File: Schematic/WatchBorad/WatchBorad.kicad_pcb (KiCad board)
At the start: 4 copper layers, 35 x 35 mm, 113 parts, among them J1 Conn_01x07_Female, J3 TYPE-C-31-M-17, M1 Motor_DC, SW1 SW_Push, SW2 SW_Push, SW3 SW_Push, SW4 SW_Push, SW5 SW_Push, U1 PQFN50P300X250X86-14N, U10 TPS62740DSST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

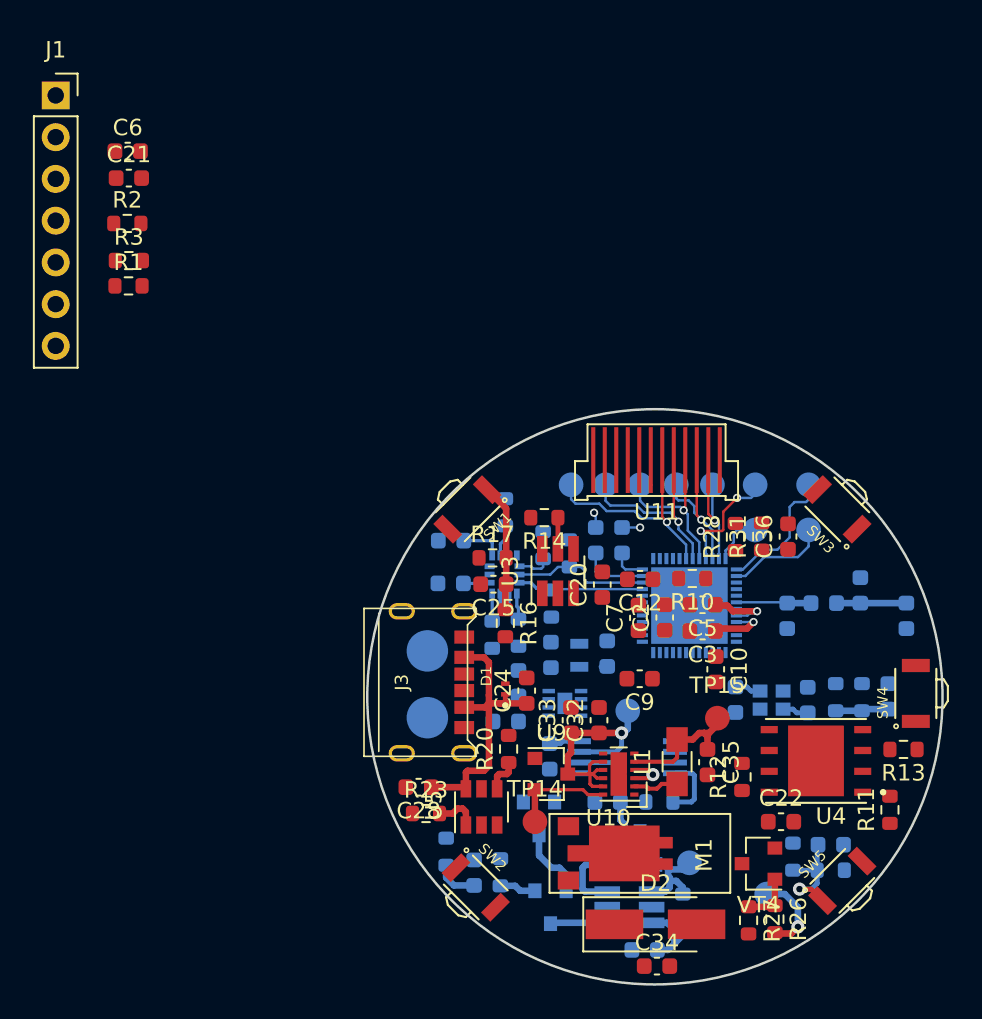
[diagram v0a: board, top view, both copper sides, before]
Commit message: Fixed board's proposals. Fixed testpoints' footprint. Fixed DRC violations. Added +5V testpoint
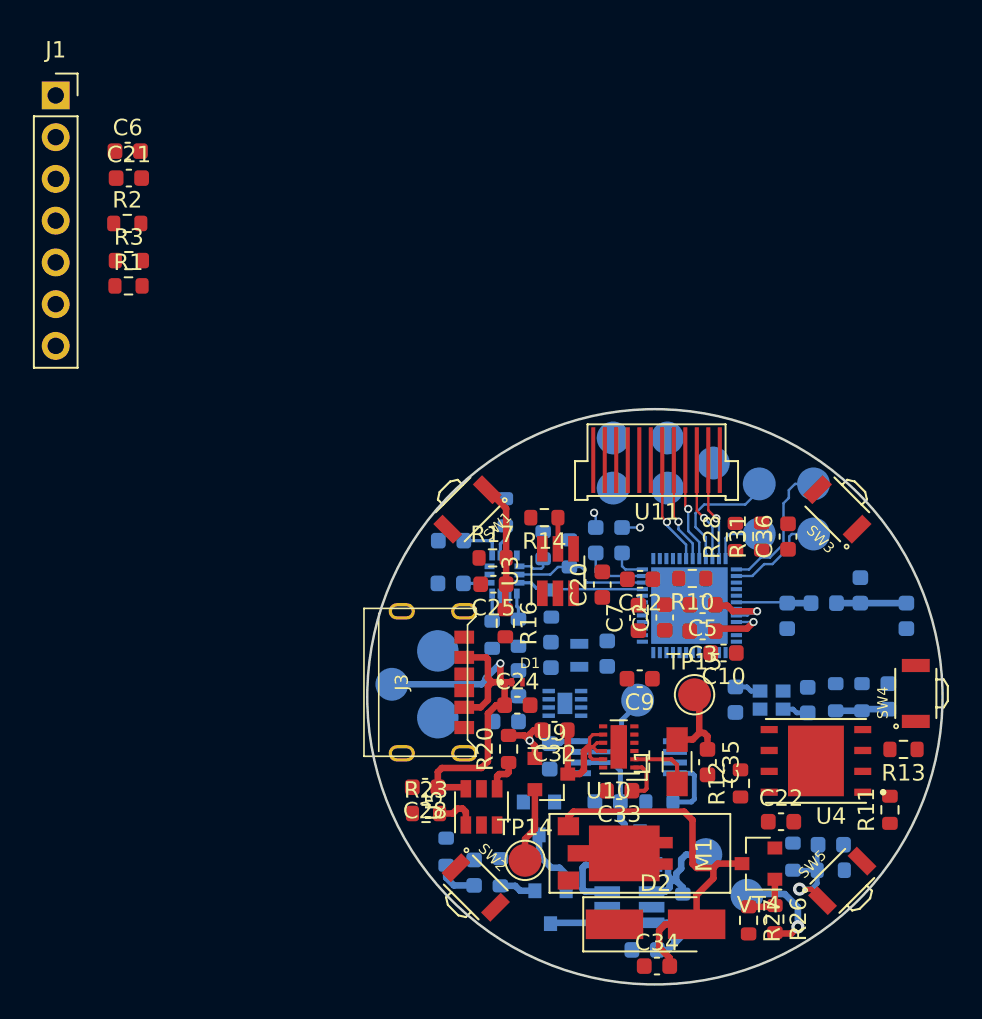
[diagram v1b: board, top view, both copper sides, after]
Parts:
- added TP5: TestPoint, TestPoint:TestPoint_Pad_D2.0mm, B.Cu at (72.9, 88.1)
- TP1, TP10, TP11, TP12, TP13, TP14, TP15, TP2, TP3, TP4, TP6, TP7, TP8, TP9: footprint Measurement_Points:Measurement_Point_Round-SMD-Pad_Small -> TestPoint:TestPoint_Pad_D2.0mm
- U1: value PQFN50P300X250X86-14N -> LSM6DSLTR
- moved C33 5.19 mm to (86.7, 94.6), turned to 180 degrees
- moved TP8 3.83 mm to (86.4, 73.2)
- moved TP7 3.30 mm to (89.7, 73.2)
- moved C32 2.78 mm to (82.8, 90.9), turned to 180 degrees
- moved TP14 2.43 mm to (81.0, 98.8)
- moved TP15 1.99 mm to (91.3, 88.8)
- moved U10 1.65 mm to (86.7, 91.9)
- moved TP10 1.33 mm to (92.5, 74.7)
- moved TP13 1.20 mm to (94.5, 101.0)
- moved TP11 1.12 mm to (92.0, 98.5)
- moved C10 1.10 mm to (93.1, 86.2), turned to 180 degrees
- moved C24 1.05 mm to (80.5, 89.4), turned to 0 degrees
- moved TP12 0.88 mm to (87.8, 89.1)
- moved D1 0.83 mm to (80.5, 88.0), turned to 0 degrees
- moved BT1 0.63 mm to (75.7, 88.1)
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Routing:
- net Net-(C34-Pad2): track 0.00 -> 23.1 mm
- net +5V: track 19.1 -> 28.8 mm, vias 0 -> 1
- net /MCU/DISP_DC: track 13.9 -> 6.59 mm
- net /MCU/DISP_CS: track 12.4 -> 6.47 mm
- net /MCU/DISP_SCLK: track 10.3 -> 6.34 mm
- net /MCU/DISP_SDA: track 9.52 -> 6.38 mm
- net +3V3: track 10.1 -> 7.29 mm
- net /MCU/DISP_RESET: track 8.47 -> 6.26 mm
- net /DCDC&PB/DCDC_VIN: track 16.7 -> 18.7 mm, vias 1 -> 0
- net /DCDC&PB/DCDC_ENABLE: track 6.22 -> 4.55 mm
- net Net-(R25-Pad2): track 6.92 -> 8.50 mm
- net GND: track 4.50 -> 5.89 mm
- net /DCDC&PB/Enable_motor: track 5.02 -> 6.25 mm
- net /DCDC&PB/L_SW_0: track 2.78 -> 3.90 mm
- net /MCU/SWD_SWO: track 7.25 -> 7.87 mm, vias 2 -> 0

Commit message: Added route for crystal
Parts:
- moved VT2 1.66 mm to (82.5, 97.8)
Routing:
- net /MCU/XC1: track 1.59 -> 9.06 mm
- net /MCU/XL2: track 0.14 -> 6.90 mm
- net /MCU/XL1: track 0.00 -> 4.96 mm
- net /MCU/XC2: track 2.30 -> 6.62 mm
- net Net-(VT1-Pad2): track 4.38 -> 2.64 mm
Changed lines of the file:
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@@
     (thickness 1.6)
     (drawings 1)
-    (tracks 323)
+    (tracks 349)
     (zones 0)
     (modules 114)
@@
   (page A4)
   (layers
-    (0 F.Cu signal)
+    (0 F.Cu signal hide)
     (1 In1.Cu power hide)
     (2 In2.Cu power hide)
-    (31 B.Cu signal hide)
+    (31 B.Cu signal)
     (32 B.Adhes user hide)
     (33 F.Adhes user hide)
@@
     (44 Edge.Cuts user)
     (45 Margin user hide)
-    (46 B.CrtYd user hide)
-    (47 F.CrtYd user)
+    (46 B.CrtYd user)
+    (47 F.CrtYd user hide)
     (48 B.Fab user hide)
     (49 F.Fab user hide)
   )
   (setup
-    (last_trace_width 0.4)
+    (last_trace_width 0.15)
     (user_trace_width 0.1)
     (user_trace_width 0.15)
@@
   )
   (module TO_SOT_Packages_SMD:SOT-23 (layer B.Cu)
-    (at 81.85 96.3 270)
+    (at 82.55 97.8 270)
     (descr "SOT-23, Standard")
     (tags SOT-23)
@@
   (segment (start 97.525 89.875) (end 98.2 89.875) (width 0.3) (layer B.Cu) (net 7))
   (segment (start 97.3 89.65) (end 97.525 89.875) (width 0.3) (layer B.Cu) (net 7))
+  (segment (start 97.415001 89.534999) (end 97.3 89.65) (width 0.15) (layer B.Cu) (net 7))
+  (segment (start 97.415001 87.915001) (end 97.415001 89.534999) (width 0.15) (layer B.Cu) (net 7))
+  (segment (start 97.05 87.55) (end 97.415001 87.915001) (width 0.15) (layer B.Cu) (net 7))
+  (segment (start 95.9 87.55) (end 97.05 87.55) (width 0.15) (layer B.Cu) (net 7))
+  (segment (start 95.65 85.9) (end 95.65 87.3) (width 0.15) (layer B.Cu) (net 7))
+  (segment (start 94.5 84.75) (end 95.65 85.9) (width 0.15) (layer B.Cu) (net 7))
+  (segment (start 95.65 87.3) (end 95.9 87.55) (width 0.15) (layer B.Cu) (net 7))
+  (segment (start 93.86 84.75) (end 94.5 84.75) (width 0.15) (layer B.Cu) (net 7))
   (segment (start 93.8 88.3) (end 93.8 88.6) (width 0.15) (layer B.Cu) (net 8))
   (segment (start 93.8 88.3) (end 94.2 88.3) (width 0.2) (layer B.Cu) (net 8))
@@
   (segment (start 94.75 88.55) (end 95.3 88.55) (width 0.3) (layer B.Cu) (net 8))
   (segment (start 94.5 88.3) (end 94.75 88.55) (width 0.3) (layer B.Cu) (net 8))
+  (segment (start 94.402002 85.15) (end 95.3 86.047998) (width 0.15) (layer B.Cu) (net 8))
+  (segment (start 93.86 85.15) (end 94.402002 85.15) (width 0.15) (layer B.Cu) (net 8))
+  (segment (start 95.3 86.047998) (end 95.3 88) (width 0.15) (layer B.Cu) (net 8))
+  (segment (start 95.3 88) (end 95.3 88.55) (width 0.15) (layer B.Cu) (net 8))
+  (segment (start 85.975 87.075) (end 86 87.05) (width 0.4) (layer B.Cu) (net 9))
+  (segment (start 84.3 87.075) (end 85.975 87.075) (width 0.4) (layer B.Cu) (net 9))
+  (segment (start 86 87.05) (end 86.2 87.05) (width 0.15) (layer B.Cu) (net 9))
+  (segment (start 86.2 87.05) (end 87.35 85.9) (width 0.15) (layer B.Cu) (net 9))
+  (segment (start 87.35 85.9) (end 87.35 85.35) (width 0.15) (layer B.Cu) (net 9))
+  (segment (start 87.55 85.15) (end 88.14 85.15) (width 0.15) (layer B.Cu) (net 9))
+  (segment (start 87.35 85.35) (end 87.55 85.15) (width 0.15) (layer B.Cu) (net 9))
   (segment (start 82.675 85.675) (end 82.575 85.575) (width 0.4) (layer B.Cu) (net 10))
+  (segment (start 84.3 85.675) (end 82.675 85.675) (width 0.4) (layer B.Cu) (net 10))
+  (segment (start 84.3 85.675) (end 84.375 85.675) (width 0.15) (layer B.Cu) (net 10))
+  (segment (start 84.3 85.675) (end 84.575 85.675) (width 0.15) (layer B.Cu) (net 10))
+  (segment (start 86.45297 86.21501) (end 86.95 85.71798) (width 0.15) (layer B.Cu) (net 10))
+  (segment (start 85.11501 86.21501) (end 86.45297 86.21501) (width 0.15) (layer B.Cu) (net 10))
+  (segment (start 84.575 85.675) (end 85.11501 86.21501) (width 0.15) (layer B.Cu) (net 10))
+  (segment (start 86.95 85.71798) (end 86.95 85.05) (width 0.15) (layer B.Cu) (net 10))
+  (segment (start 87.25 84.75) (end 88.14 84.75) (width 0.15) (layer B.Cu) (net 10))
+  (segment (start 86.95 85.05) (end 87.25 84.75) (width 0.15) (layer B.Cu) (net 10))
   (segment (start 87.05 99.1) (end 87.05 96.65) (width 0.4) (layer B.Cu) (net 11))
   (segment (start 86.8 96.4) (end 86.8 95.3) (width 0.4) (layer B.Cu) (net 11))
@@
   (segment (start 82.6 102.65) (end 82.55 102.7) (width 0.4) (layer B.Cu) (net 24))
   (segment (start 86 102.65) (end 82.6 102.65) (width 0.4) (layer B.Cu) (net 24))
-  (segment (start 81.85 97.3) (end 81.85 98.55) (width 0.4) (layer B.Cu) (net 25))
-  (segment (start 81.85 98.55) (end 82.6 99.3) (width 0.4) (layer B.Cu) (net 25))
-  (segment (start 82.6 99.3) (end 83.1 99.3) (width 0.4) (layer B.Cu) (net 25))
-  (segment (start 83.5 99.7) (end 83.5 100.7) (width 0.4) (layer B.Cu) (net 25))
-  (segment (start 83.1 99.3) (end 83.5 99.7) (width 0.4) (layer B.Cu) (net 25))
+  (segment (start 83.5 100.7) (end 82.9 100.7) (width 0.4) (layer B.Cu) (net 25))
+  (segment (start 82.9 100.7) (end 82.55 100.35) (width 0.4) (layer B.Cu) (net 25))
+  (segment (start 82.55 98.8) (end 82.55 100.35) (width 0.4) (layer B.Cu) (net 25))
   (segment (start 94.5 84.75) (end 94.9 84.35) (width 0.4) (layer F.Cu) (net 27))
   (via (at 94.9 84.35) (size 0.5) (drill 0.3) (layers F.Cu B.Cu) (net 27))

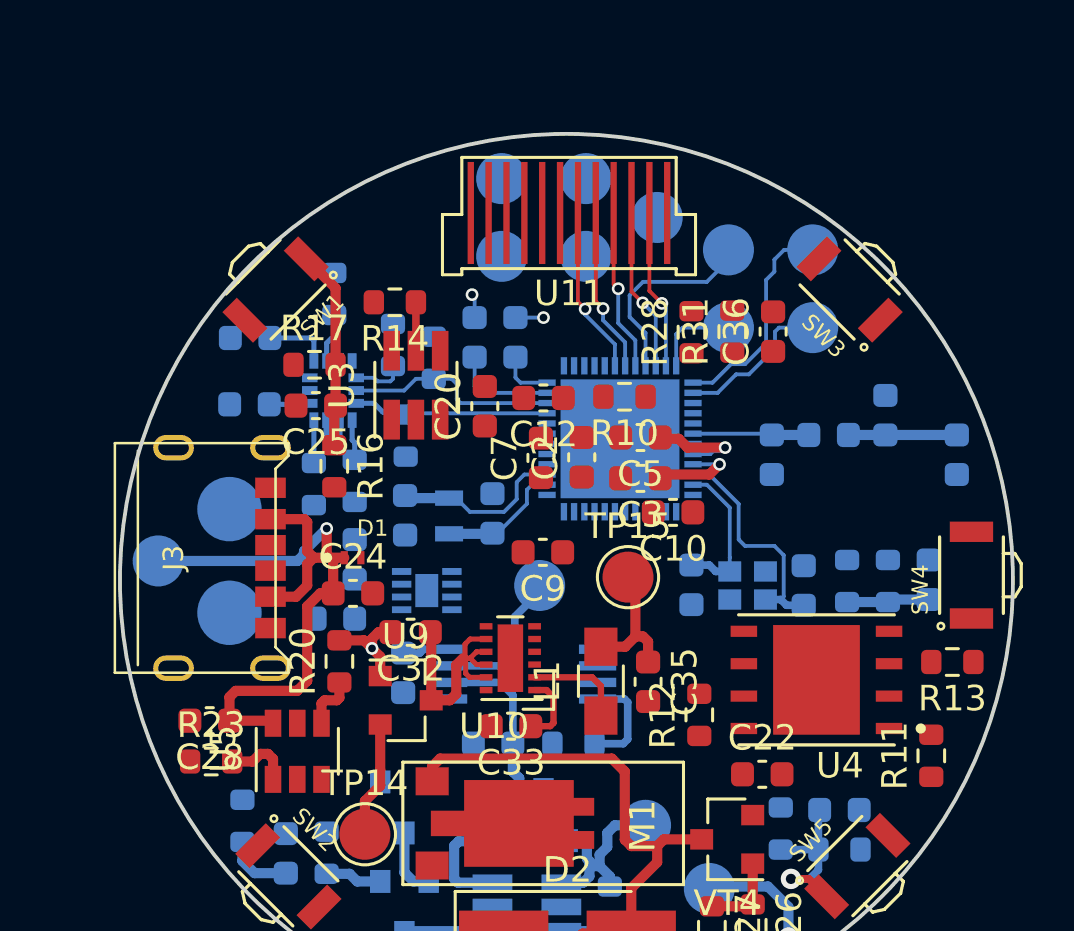
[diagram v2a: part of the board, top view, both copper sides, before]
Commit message: Added route for display testpoints
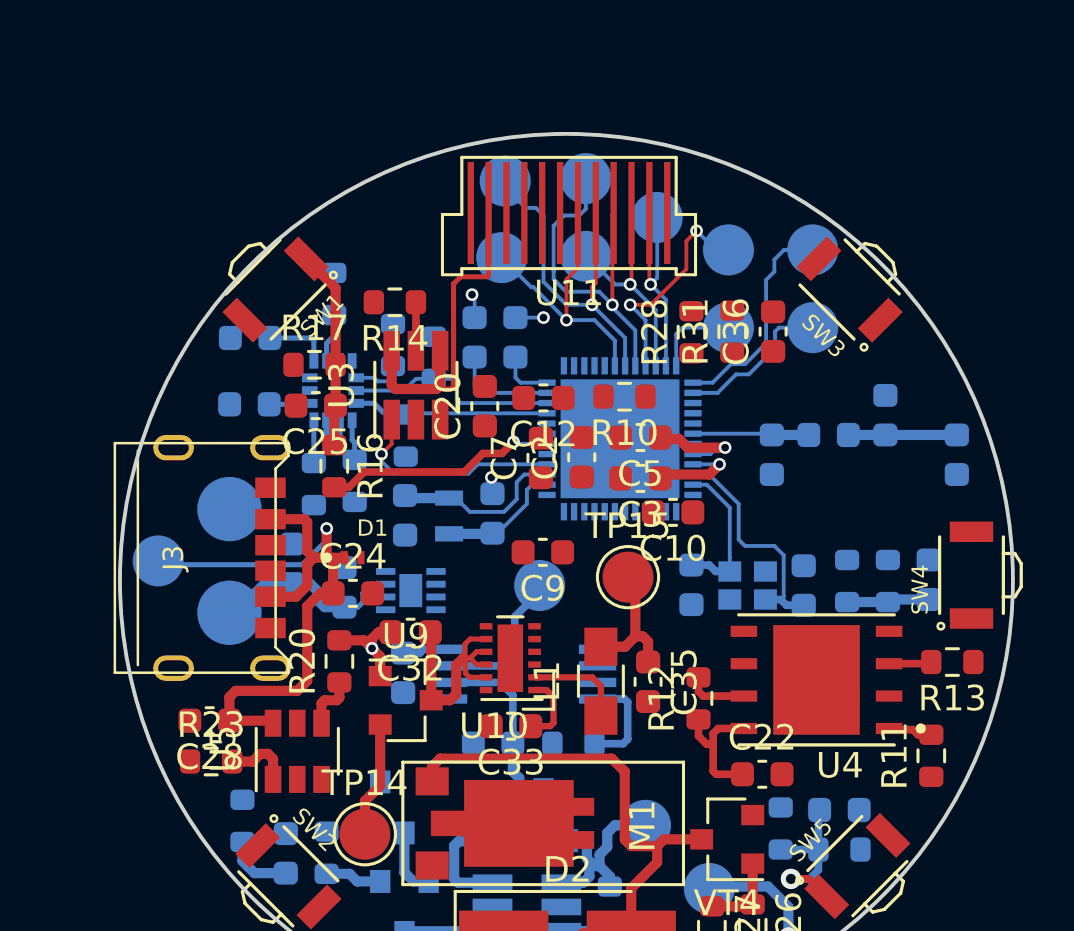
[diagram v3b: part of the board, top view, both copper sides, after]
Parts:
- moved TP8 3.10 mm to (86.4, 76.2)
- moved TP9 2.95 mm to (86.5, 73.2)
- moved C23 2.46 mm to (78.2, 88.2)
- moved C27 1.28 mm to (80.2, 89.2), turned to 90 degrees
- moved R12 0.65 mm to (94.1, 93.5)
- moved U6 0.62 mm to (82.8, 89.3)
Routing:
- net /MCU/LEDK: track 0.00 -> 13.4 mm
- net /MCU/PB_2_MCU: track 0.00 -> 9.13 mm, vias 0 -> 1
- net +BATT: track 5.10 -> 13.8 mm
- net /MCU/Backlight_EN_DIM: track 0.00 -> 8.64 mm, vias 0 -> 1
- net /MCU/DISP_SCLK: track 6.34 -> 14.0 mm
- net /MCU/DISP_CS: track 6.47 -> 13.7 mm
- net +3V3: track 7.29 -> 12.6 mm
- net /MCU/DISP_DC: track 6.59 -> 11.2 mm
- net /MCU/DISP_RESET: track 6.26 -> 8.99 mm
- net Net-(R12-Pad2): track 0.00 -> 2.41 mm
- net /MCU/DISP_SDA: track 6.38 -> 8.62 mm
- net /MCU/FLASH_CS: track 0.00 -> 1.76 mm
- net Net-(R13-Pad2): track 0.00 -> 1.68 mm
- net /MCU/SWD_SWO: track 7.87 -> 9.05 mm, vias 0 -> 2
- net GND: track 5.89 -> 6.54 mm, vias 3 -> 4
